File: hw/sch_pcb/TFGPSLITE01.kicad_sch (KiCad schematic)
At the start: 26 parts, among them IC1 CAM-M8Q, J1 SM06B-GHS-TB, J2 SM04B-GHS-TB, M1 HOLE, M2 HOLE, M3 HOLE, M4 HOLE, U1 MIC5504-3.3YM5

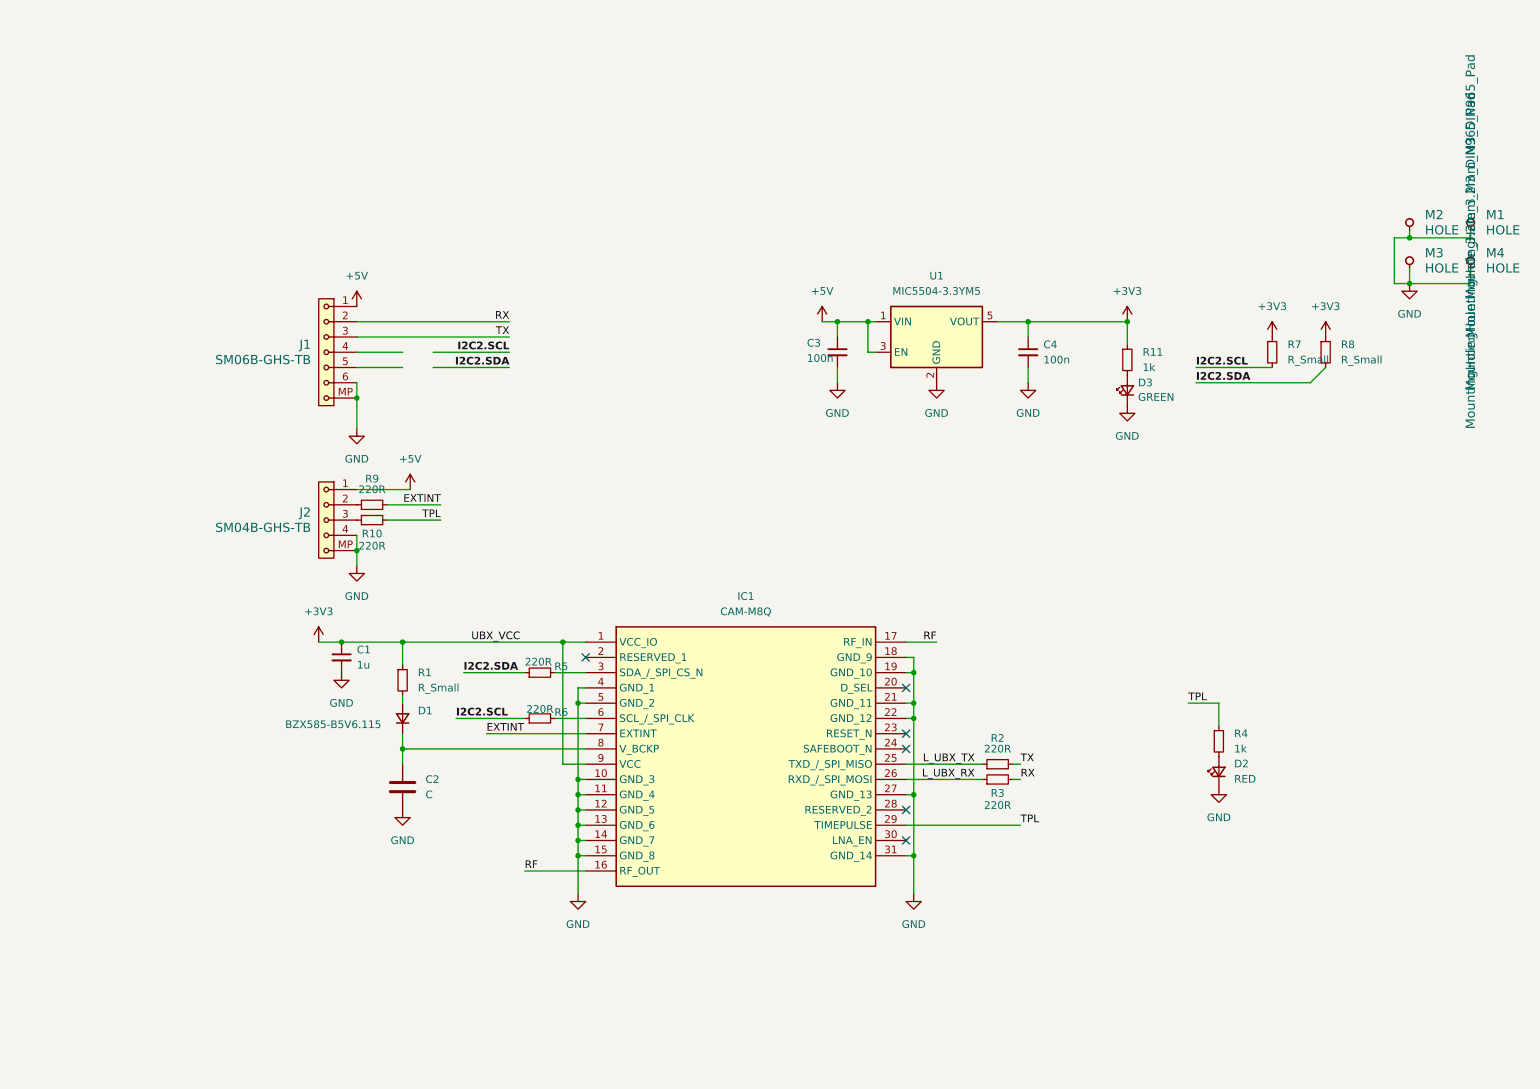
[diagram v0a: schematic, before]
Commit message: solve DRC, silkscreen
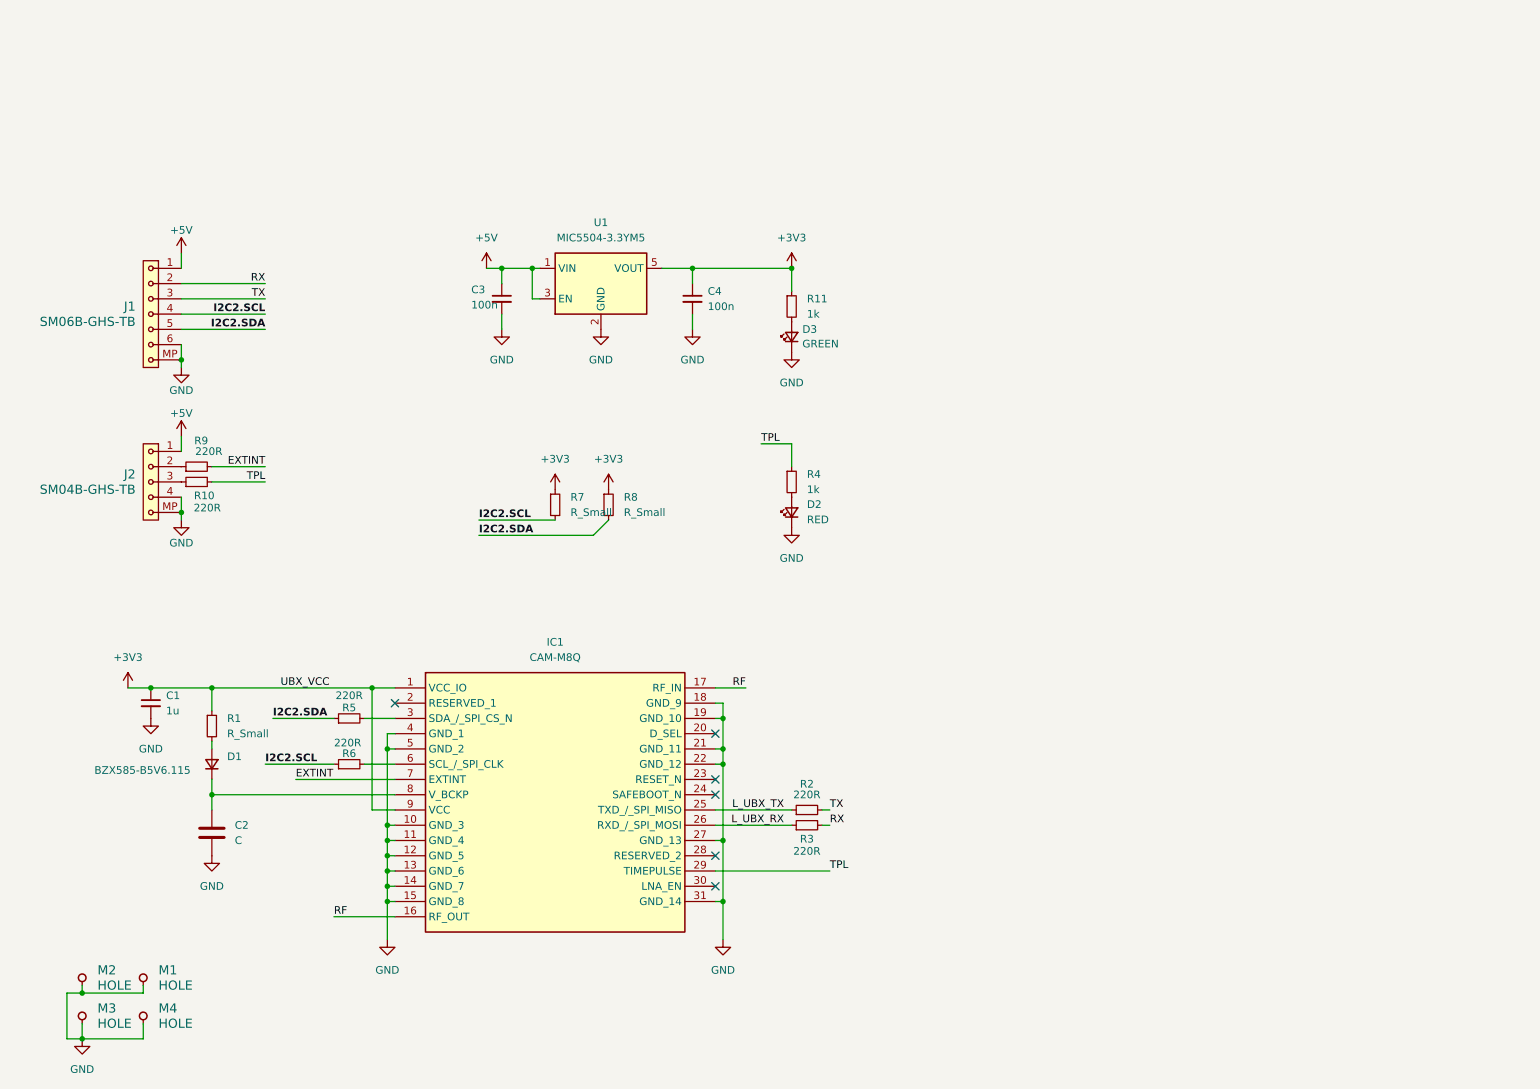
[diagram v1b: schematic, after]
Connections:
- net I2C2.SCL: now also J1.4
- net I2C2.SDA: now also J1.5
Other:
- moved on the sheet: C1, C2, C3, C4, D1, D2, D3, IC1, J1, J2, M1, M2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
